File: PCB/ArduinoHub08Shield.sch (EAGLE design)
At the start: 2 parts

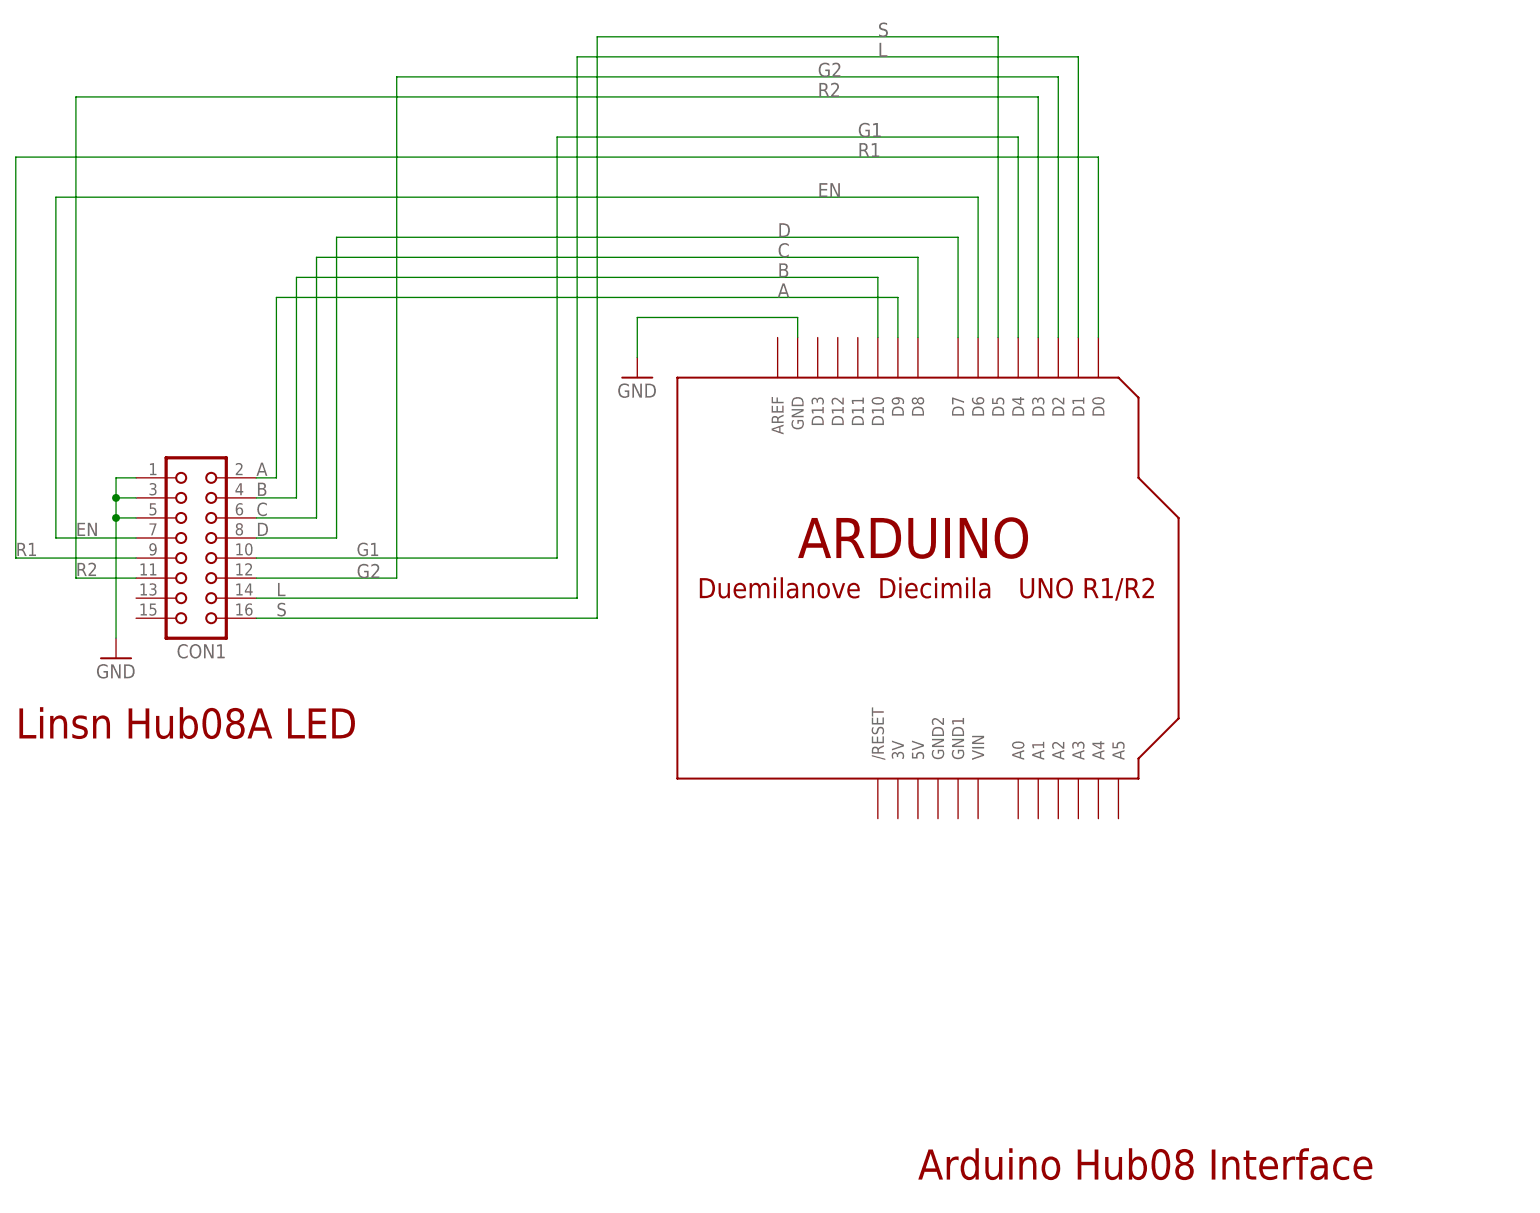
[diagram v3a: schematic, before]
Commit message: Hardware Update (Schematic/PCB and Hardware.h)
Because we cant use the digital pins 0,1 on Yun, we updated
the schematic and layout to use different pins.

Now the A-D address lines are also on the high nibble of
PORTB, which leave some room for even more tuning of the
ISR.
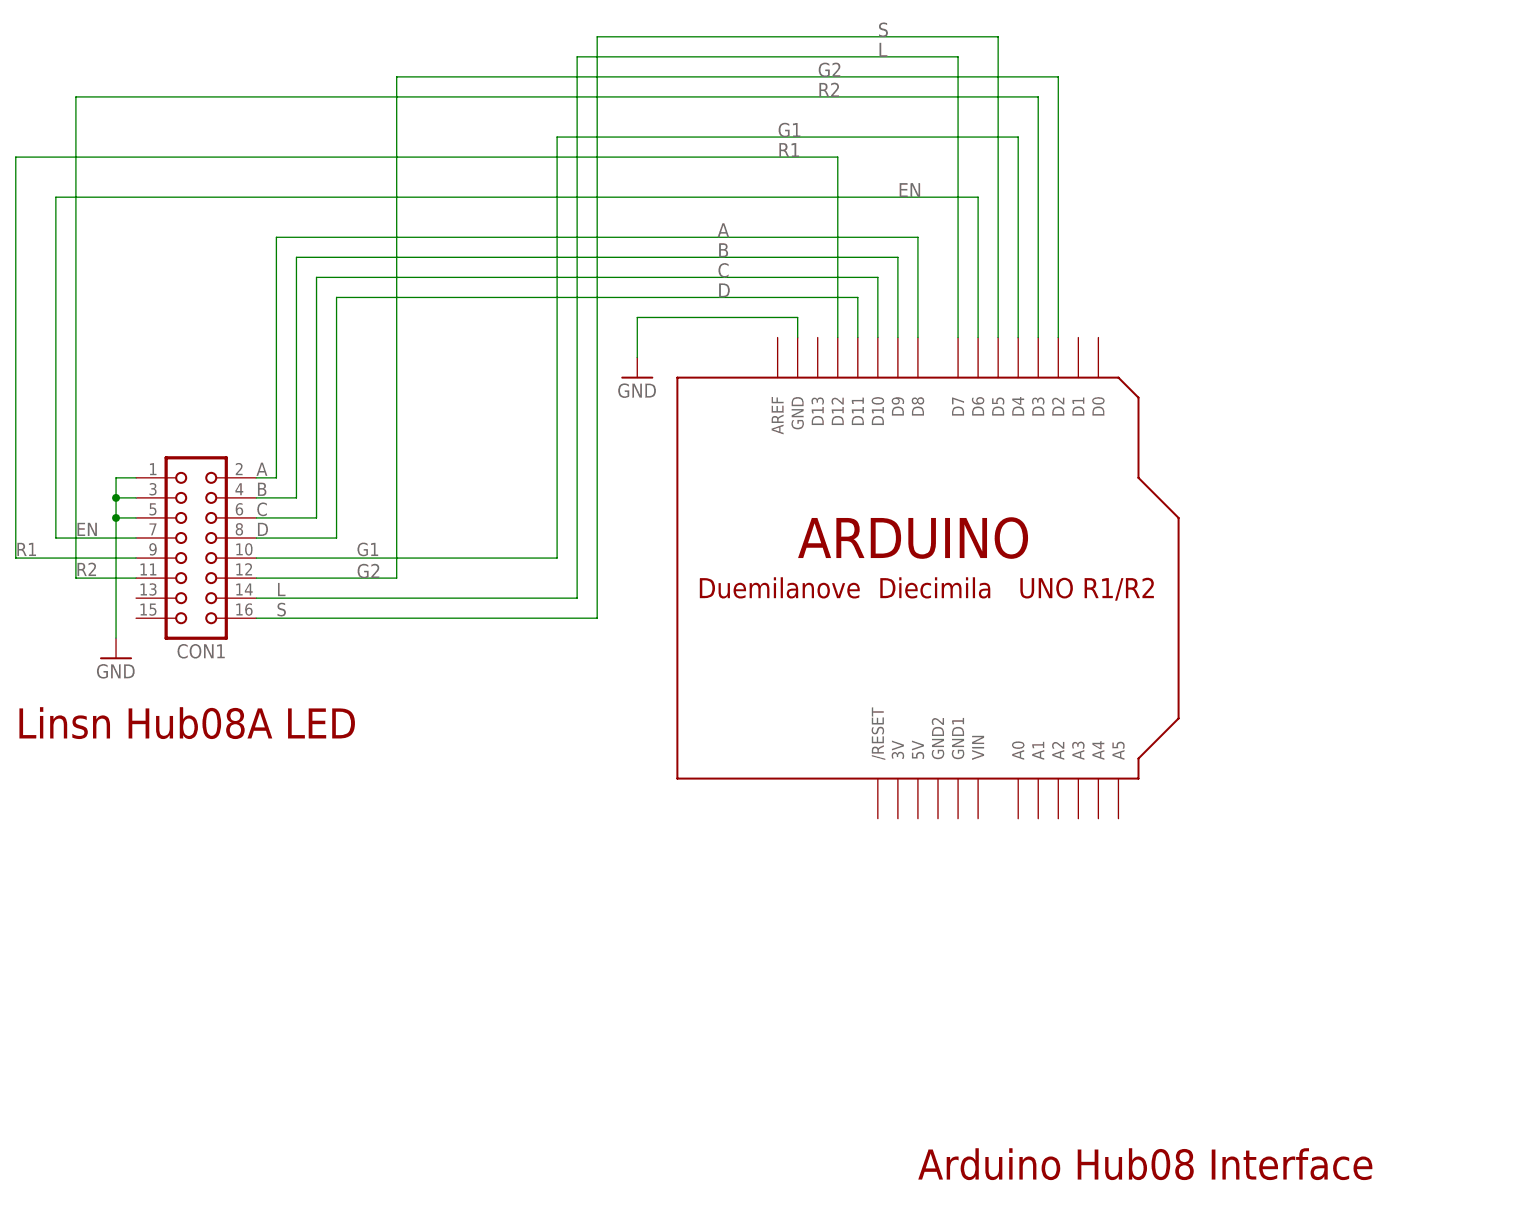
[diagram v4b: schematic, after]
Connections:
- net A: now also U$1.D8; no longer U$1.D9
- net B: now also U$1.D9; no longer U$1.D10
- net C: now also U$1.D10; no longer U$1.D8
- net D: now also U$1.D11; no longer U$1.D7
- net L: now also U$1.D7; no longer U$1.D1
- net R1: now also U$1.D12; no longer U$1.D0
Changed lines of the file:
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@@
 <label x="60.96" y="106.934" size="1.6764" layer="95"/>
 <wire x1="60.96" y1="106.68" x2="60.96" y2="157.48" width="0.1524" layer="91"/>
-<wire x1="60.96" y1="157.48" x2="198.12" y2="157.48" width="0.1524" layer="91"/>
-<label x="167.64" y="157.48" size="1.778" layer="95"/>
-<pinref part="U$1" gate="G$1" pin="D0"/>
-<wire x1="198.12" y1="157.48" x2="198.12" y2="134.62" width="0.1524" layer="91"/>
+<pinref part="U$1" gate="G$1" pin="D12"/>
+<wire x1="60.96" y1="157.48" x2="165.1" y2="157.48" width="0.1524" layer="91"/>
+<wire x1="165.1" y1="157.48" x2="165.1" y2="134.62" width="0.1524" layer="91"/>
+<label x="157.48" y="157.48" size="1.778" layer="95"/>
 </segment>
 </net>
@@
 <label x="93.98" y="101.854" size="1.6764" layer="95"/>
 <wire x1="132.08" y1="101.6" x2="132.08" y2="170.18" width="0.1524" layer="91"/>
-<wire x1="132.08" y1="170.18" x2="195.58" y2="170.18" width="0.1524" layer="91"/>
-<pinref part="U$1" gate="G$1" pin="D1"/>
-<wire x1="195.58" y1="170.18" x2="195.58" y2="134.62" width="0.1524" layer="91"/>
+<pinref part="U$1" gate="G$1" pin="D7"/>
+<wire x1="132.08" y1="170.18" x2="180.34" y2="170.18" width="0.1524" layer="91"/>
+<wire x1="180.34" y1="170.18" x2="180.34" y2="134.62" width="0.1524" layer="91"/>
 <label x="170.18" y="170.18" size="1.778" layer="95"/>
 </segment>
@@
 <wire x1="91.44" y1="109.22" x2="101.6" y2="109.22" width="0.1524" layer="91"/>
 <label x="91.44" y="109.474" size="1.6764" layer="95"/>
-<wire x1="101.6" y1="109.22" x2="101.6" y2="147.32" width="0.1524" layer="91"/>
-<wire x1="101.6" y1="147.32" x2="180.34" y2="147.32" width="0.1524" layer="91"/>
-<label x="157.48" y="147.32" size="1.778" layer="95"/>
-<pinref part="U$1" gate="G$1" pin="D7"/>
-<wire x1="180.34" y1="147.32" x2="180.34" y2="134.62" width="0.1524" layer="91"/>
+<wire x1="101.6" y1="109.22" x2="101.6" y2="139.7" width="0.1524" layer="91"/>
+<wire x1="101.6" y1="139.7" x2="167.64" y2="139.7" width="0.1524" layer="91"/>
+<pinref part="U$1" gate="G$1" pin="D11"/>
+<wire x1="167.64" y1="139.7" x2="167.64" y2="134.62" width="0.1524" layer="91"/>
+<label x="149.86" y="139.7" size="1.778" layer="95"/>
 </segment>
 </net>
@@
 <wire x1="91.44" y1="111.76" x2="99.06" y2="111.76" width="0.1524" layer="91"/>
 <label x="91.44" y="112.014" size="1.6764" layer="95"/>
-<wire x1="99.06" y1="111.76" x2="99.06" y2="144.78" width="0.1524" layer="91"/>
-<wire x1="99.06" y1="144.78" x2="175.26" y2="144.78" width="0.1524" layer="91"/>
-<label x="157.48" y="144.78" size="1.778" layer="95"/>
-<pinref part="U$1" gate="G$1" pin="D8"/>
-<wire x1="175.26" y1="144.78" x2="175.26" y2="134.62" width="0.1524" layer="91"/>
+<wire x1="99.06" y1="111.76" x2="99.06" y2="142.24" width="0.1524" layer="91"/>
+<wire x1="99.06" y1="142.24" x2="170.18" y2="142.24" width="0.1524" layer="91"/>
+<pinref part="U$1" gate="G$1" pin="D10"/>
+<wire x1="170.18" y1="142.24" x2="170.18" y2="134.62" width="0.1524" layer="91"/>
+<label x="149.86" y="142.24" size="1.778" layer="95"/>
 </segment>
 </net>
@@
 <wire x1="91.44" y1="114.3" x2="96.52" y2="114.3" width="0.1524" layer="91"/>
 <label x="91.44" y="114.554" size="1.6764" layer="95"/>
-<wire x1="96.52" y1="114.3" x2="96.52" y2="142.24" width="0.1524" layer="91"/>
-<wire x1="96.52" y1="142.24" x2="170.18" y2="142.24" width="0.1524" layer="91"/>
-<label x="157.48" y="142.24" size="1.778" layer="95"/>
-<pinref part="U$1" gate="G$1" pin="D10"/>
-<wire x1="170.18" y1="142.24" x2="170.18" y2="134.62" width="0.1524" layer="91"/>
+<wire x1="96.52" y1="114.3" x2="96.52" y2="144.78" width="0.1524" layer="91"/>
+<wire x1="96.52" y1="144.78" x2="172.72" y2="144.78" width="0.1524" layer="91"/>
+<pinref part="U$1" gate="G$1" pin="D9"/>
+<wire x1="172.72" y1="144.78" x2="172.72" y2="134.62" width="0.1524" layer="91"/>
+<label x="149.86" y="144.78" size="1.778" layer="95"/>
 </segment>
 </net>
@@
 <wire x1="93.98" y1="116.84" x2="91.44" y2="116.84" width="0.1524" layer="91"/>
 <label x="91.44" y="117.094" size="1.6764" layer="95"/>
-<wire x1="93.98" y1="116.84" x2="93.98" y2="139.7" width="0.1524" layer="91"/>
-<wire x1="93.98" y1="139.7" x2="172.72" y2="139.7" width="0.1524" layer="91"/>
-<label x="157.48" y="139.7" size="1.778" layer="95"/>
-<pinref part="U$1" gate="G$1" pin="D9"/>
-<wire x1="172.72" y1="139.7" x2="172.72" y2="134.62" width="0.1524" layer="91"/>
+<wire x1="93.98" y1="116.84" x2="93.98" y2="147.32" width="0.1524" layer="91"/>
+<wire x1="93.98" y1="147.32" x2="175.26" y2="147.32" width="0.1524" layer="91"/>
+<pinref part="U$1" gate="G$1" pin="D8"/>
+<wire x1="175.26" y1="147.32" x2="175.26" y2="134.62" width="0.1524" layer="91"/>
+<label x="149.86" y="147.32" size="1.778" layer="95"/>
 </segment>
 </net>
@@
 <wire x1="66.04" y1="109.22" x2="66.04" y2="152.4" width="0.1524" layer="91"/>
 <wire x1="66.04" y1="152.4" x2="182.88" y2="152.4" width="0.1524" layer="91"/>
-<label x="162.56" y="152.4" size="1.778" layer="95"/>
+<label x="172.72" y="152.4" size="1.778" layer="95"/>
 <pinref part="U$1" gate="G$1" pin="D6"/>
 <wire x1="182.88" y1="152.4" x2="182.88" y2="134.62" width="0.1524" layer="91"/>
@@
 <wire x1="129.54" y1="106.68" x2="129.54" y2="160.02" width="0.1524" layer="91"/>
 <wire x1="129.54" y1="160.02" x2="187.96" y2="160.02" width="0.1524" layer="91"/>
-<label x="167.64" y="160.02" size="1.778" layer="95"/>
+<label x="157.48" y="160.02" size="1.778" layer="95"/>
 <pinref part="U$1" gate="G$1" pin="D4"/>
 <wire x1="187.96" y1="160.02" x2="187.96" y2="134.62" width="0.1524" layer="91"/>
